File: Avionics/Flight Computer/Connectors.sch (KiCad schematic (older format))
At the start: 3 parts, among them J1 ERF8-040-05.0-S-DV-K, J2 ERF8-040-05.0-S-DV-K, J3 473460001

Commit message: Built outputs and added manufacturing part numbers to make BOM search easier.
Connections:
- net 900-DIO-17: now also J2.73 (P73); no longer J2.71 (P71)
- net 900-DIO-18: now also J2.71 (P71); no longer J2.69 (P69)
- net 900-DIO-21: now also J2.69 (P69); no longer J2.73 (P73)
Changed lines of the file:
@@
 $EndComp
 $Comp
-L VUSB #PWR129
+L VUSB #PWR0147
 U 1 1 58B8BBBA
 P 1600 1150
-F 0 "#PWR129" H -400 -250 50  0001 C CNN
+F 0 "#PWR0147" H -400 -250 50  0001 C CNN
 F 1 "VUSB" H 1615 1323 50  0000 C CNN
 F 2 "" H -400 -100 50  0001 C CNN
@@
 	1600 1250 1600 1150
 $Comp
-L GND #PWR128
+L GND #PWR0148
 U 1 1 58B8BD69
 P 1100 1900
-F 0 "#PWR128" H -800 50  50  0001 C CNN
+F 0 "#PWR0148" H -800 50  50  0001 C CNN
 F 1 "GND" H 1105 1727 50  0000 C CNN
 F 2 "" H -800 300 50  0001 C CNN
@@
 Must be connected to open drain\n
 $Comp
-L +BATT #PWR133
+L +BATT #PWR0149
 U 1 1 58DB91A4
 P 4950 1600
-F 0 "#PWR133" H 3900 -1300 50  0001 C CNN
+F 0 "#PWR0149" H 3900 -1300 50  0001 C CNN
 F 1 "+BATT" H 4965 1773 50  0000 C CNN
 F 2 "" H 3900 -1150 50  0001 C CNN
@@
 	9500 2600 10000 2600
 $Comp
-L GND #PWR132
+L GND #PWR0150
 U 1 1 58DD26EA
 P 4700 1400
-F 0 "#PWR132" H 750 -2300 50  0001 C CNN
+F 0 "#PWR0150" H 750 -2300 50  0001 C CNN
 F 1 "GND" H 4705 1227 50  0000 C CNN
 F 2 "" H 750 -2050 50  0001 C CNN
@@
 Wire Wire Line
 	7350 5050 7950 5050
+Text Label 7350 4750 0    60   ~ 0
+900-DIO-21
 Text Label 7350 4950 0    60   ~ 0
-900-DIO-21
+900-DIO-17
 Text Label 7350 4850 0    60   ~ 0
-900-DIO-17
-Text Label 7350 4750 0    60   ~ 0
 900-DIO-18
 Text Label 6850 5150 2    60   ~ 0
@@
 	7350 2750 8150 2750
 $Comp
-L GND #PWR135
+L GND #PWR0151
 U 1 1 58BDD19A
 P 8150 2950
-F 0 "#PWR135" H 4200 -750 50  0001 C CNN
+F 0 "#PWR0151" H 4200 -750 50  0001 C CNN
 F 1 "GND" H 8155 2777 50  0000 C CNN
 F 2 "" H 4200 -500 50  0001 C CNN
@@
 Connection ~ 3100 2300
 $Comp
-L GND #PWR131
+L GND #PWR0152
 U 1 1 58BDD20C
 P 3100 2500
-F 0 "#PWR131" H -850 -1200 50  0001 C CNN
+F 0 "#PWR0152" H -850 -1200 50  0001 C CNN
 F 1 "GND" H 3105 2327 50  0000 C CNN
 F 2 "" H -850 -950 50  0001 C CNN
@@
 $EndComp
 $Comp
-L PWR_FLAG #FLG21
+L PWR_FLAG #FLG0153
 U 1 1 58BE5320
 P 4850 1700
-F 0 "#FLG21" H -800 275 50  0001 C CNN
+F 0 "#FLG0153" H -800 275 50  0001 C CNN
 F 1 "PWR_FLAG" H 4850 1873 50  0000 C CNN
 F 2 "" H -800 200 50  0001 C CNN
@@
 Connection ~ 4850 1700
 $Comp
-L PWR_FLAG #FLG19
+L PWR_FLAG #FLG0154
 U 1 1 58BE5430
 P 1900 1250
-F 0 "#FLG19" H -3750 -175 50  0001 C CNN
+F 0 "#FLG0154" H -3750 -175 50  0001 C CNN
 F 1 "PWR_FLAG" H 1900 1424 50  0000 C CNN
 F 2 "" H -3750 -250 50  0001 C CNN
@@
 Connection ~ 1600 1250
 $Comp
-L PWR_FLAG #FLG20
+L PWR_FLAG #FLG0155
 U 1 1 58BEF4A7
 P 3100 2400
-F 0 "#FLG20" H -2550 975 50  0001 C CNN
+F 0 "#FLG0155" H -2550 975 50  0001 C CNN
 F 1 "PWR_FLAG" V 3100 2528 50  0000 L CNN
 F 2 "" H -2550 900 50  0001 C CNN
@@
 	3100 2300 3100 2200
 $Comp
-L +3.3V #PWR130
+L +3.3V #PWR0156
 U 1 1 58BFD0A3
 P 3100 2200
-F 0 "#PWR130" H 100 100 50  0001 C CNN
+F 0 "#PWR0156" H 100 100 50  0001 C CNN
 F 1 "+3.3V" H 3115 2373 50  0000 C CNN
 F 2 "" H 100 250 50  0001 C CNN
@@
 $EndComp
 $Comp
-L +3.3V #PWR134
+L +3.3V #PWR0157
 U 1 1 58BFD1FD
 P 8150 2650
-F 0 "#PWR134" H 5150 550 50  0001 C CNN
+F 0 "#PWR0157" H 5150 550 50  0001 C CNN
 F 1 "+3.3V" H 8165 2823 50  0000 C CNN
 F 2 "" H 5150 700 50  0001 C CNN

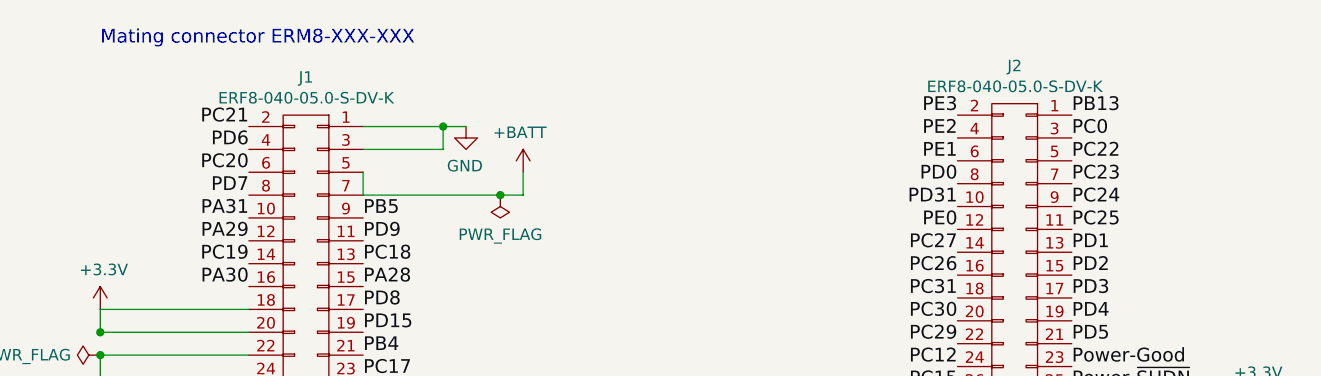
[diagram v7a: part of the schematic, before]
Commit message: Fixed connector part number
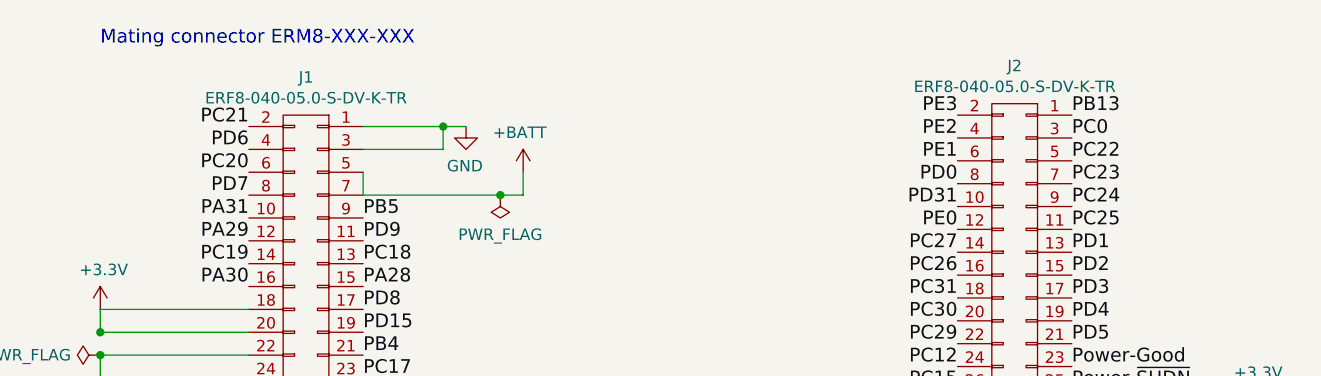
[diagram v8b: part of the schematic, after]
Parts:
- J1, J2: value ERF8-040-05.0-S-DV-K -> ERF8-040-05.0-S-DV-K-TR
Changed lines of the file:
@@
 P 4000 3350
 F 0 "J1" H 4000 5515 50  0000 C CNN
-F 1 "ERF8-040-05.0-S-DV-K" H 4000 5424 50  0000 C CNN
+F 1 "ERF8-040-05.0-S-DV-K-TR" H 4000 5424 50  0000 C CNN
 F 2 "Connectors_Samtec:ERF8-040-05.0-S-DV-K" H -550 200 50  0001 C CNN
 F 3 "http://suddendocs.samtec.com/prints/erf8-xxx-xx.x-x-dv-xxxx-tr-mkt.pdf" H -550 200 50  0001 C CNN
@@
 P 7100 3300
 F 0 "J2" H 7100 5465 50  0000 C CNN
-F 1 "ERF8-040-05.0-S-DV-K" H 7100 5374 50  0000 C CNN
+F 1 "ERF8-040-05.0-S-DV-K-TR" H 7100 5374 50  0000 C CNN
 F 2 "Connectors_Samtec:ERF8-040-05.0-S-DV-K" H 2550 150 50  0001 C CNN
 F 3 "http://suddendocs.samtec.com/prints/erf8-xxx-xx.x-x-dv-xxxx-tr-mkt.pdf" H 2550 150 50  0001 C CNN
